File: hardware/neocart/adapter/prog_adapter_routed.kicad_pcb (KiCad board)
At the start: 2 copper layers, 174 x 134 mm, 79 parts, among them J1 FPGA_U2, J2 TO_CHA, J3 FPGA_U1, J4 microSD, U1 74LVC245, U10 74HC165, U2 74LVC245, U3 74LVC245, U4 74HC165, U5 74HC165, U6 74HC165, U7 74HC165, U8 74HC165, U9 74HC165

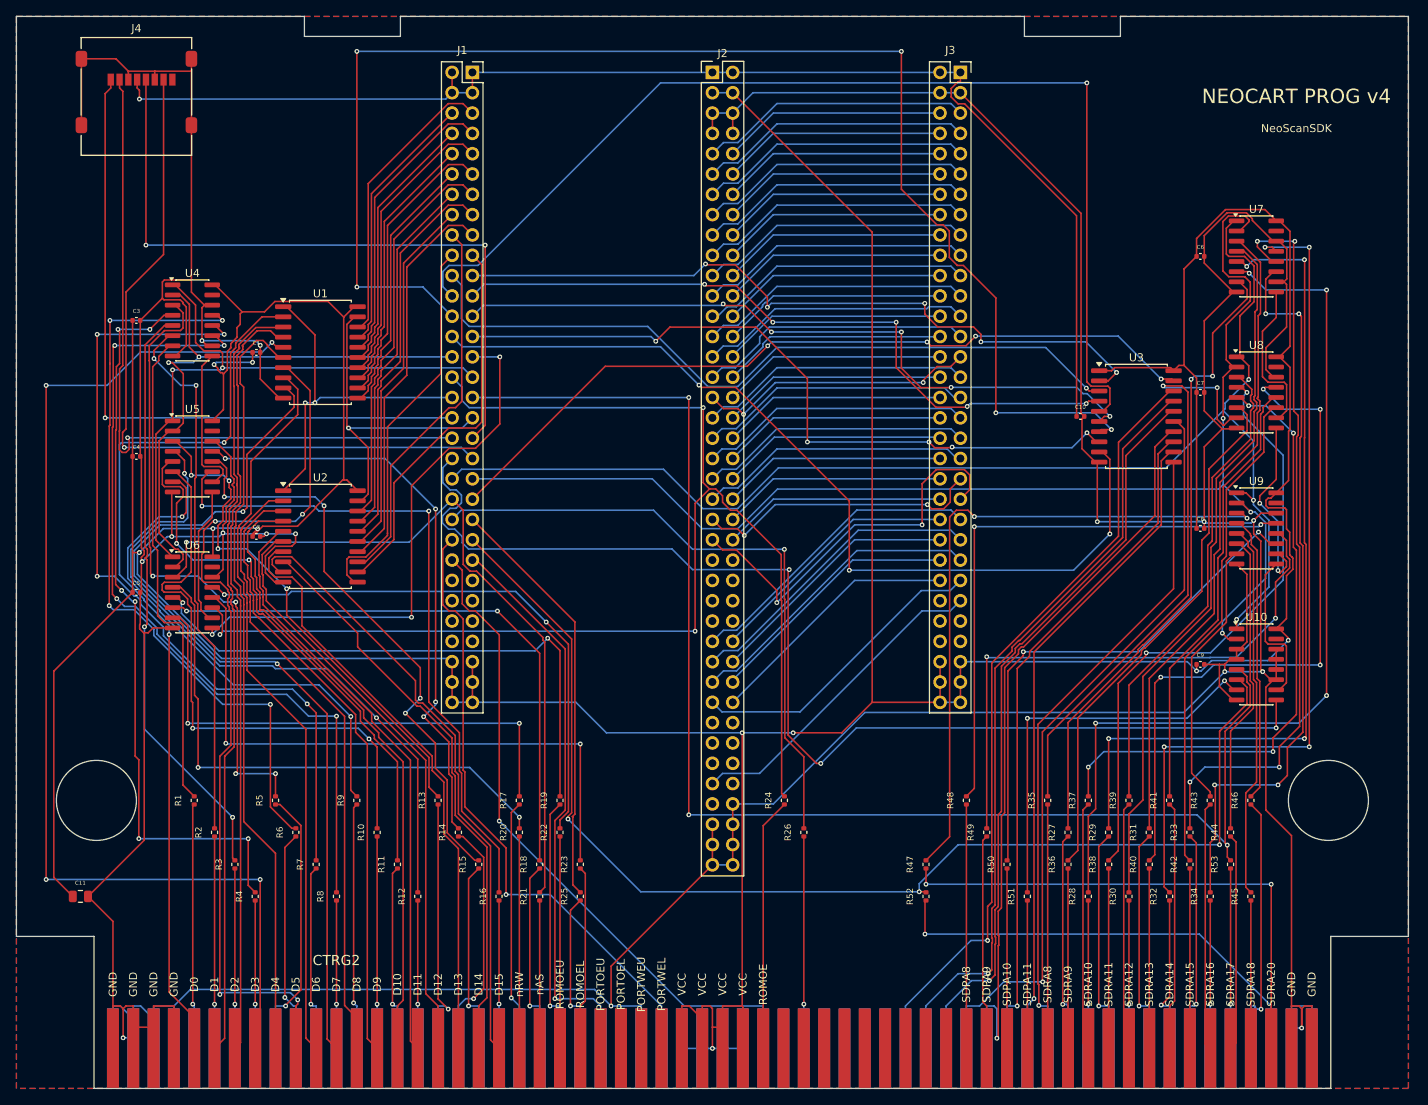
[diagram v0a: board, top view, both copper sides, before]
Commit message: NeoCart final routed PCBs + JLCPCB Gerbers — ready to order
Fixed J1 GND pins (60,62,64) from QMTech schematic — FPGA now has
ground through both headers. Re-routed with Freerouting 2.0.1 (Java 21,
multi-thread). GND routed as signal net, not just copper pour.

DRC clean:
- PROG: 143 violations (121 gold finger edge + 22 text cosmetic), 0 unconnected
- CHA:  152 violations (120 gold finger edge + 32 cosmetic), 0 unconnected
- 0 starved thermals, 0 shorts, 0 clearance errors

Chip verification: all 10 ICs power correct, all signal pins connected,
J1 GND confirmed on pins 60/62/64, J2 aligned between boards.

Gerbers: neocart_prog_gerbers.zip, neocart_cha_gerbers.zip
Order settings: 2-layer, 1.6mm, ENIG, gold fingers Yes, 45° chamfer.

Co-Authored-By: Claude Opus 4.6 (1M context) <noreply@anthropic.com>
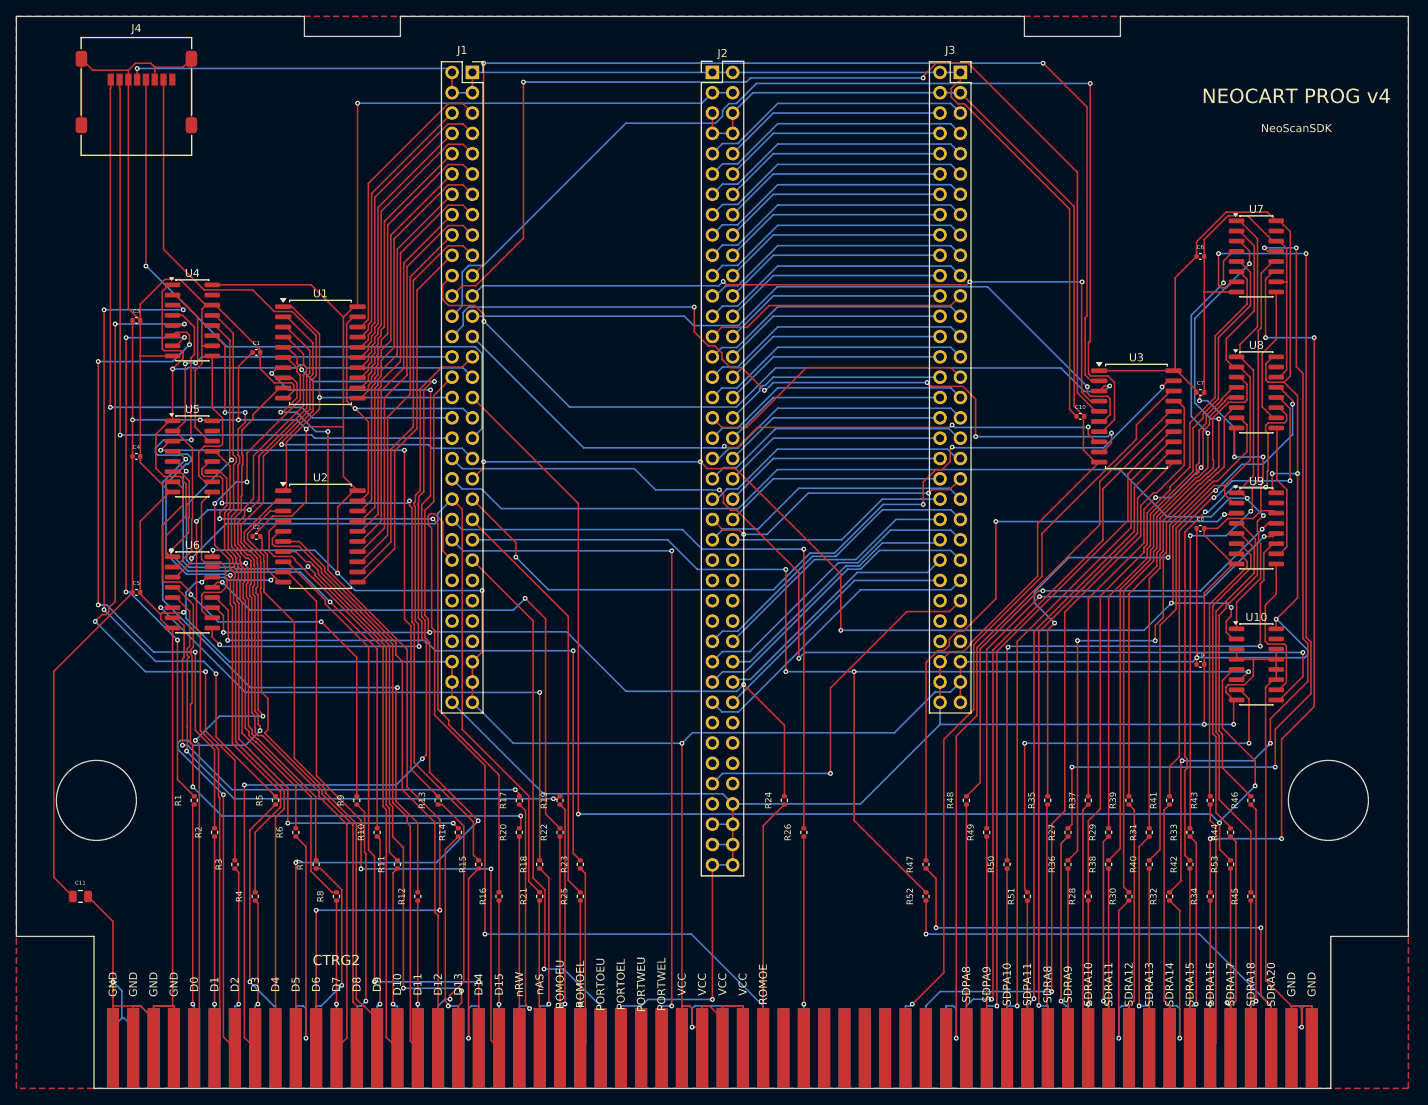
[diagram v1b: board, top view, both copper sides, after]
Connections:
- J1 pad 60: VCC_5V -> GND
- J1 pad 62: VCC_5V -> GND
- J1 pad 64: VCC_5V -> GND
- J3 pad 60: VCC_5V -> GND
- J3 pad 62: VCC_5V -> GND
- J3 pad 64: VCC_5V -> GND
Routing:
- net FSD0: track 91.9 -> 140.5 mm, vias 5 -> 2
- net ROMOE_R: track 170.0 -> 122.1 mm
- net GND: track 821.5 -> 868.1 mm, vias 15 -> 11
- net SDRA0_R: track 79.7 -> 117.2 mm, vias 2 -> 4
- net FSD5: track 178.9 -> 142.0 mm, vias 5 -> 1
- net SDRA1_R: track 114.7 -> 86.6 mm, vias 4 -> 0
- net SDRA2_R: track 104.8 -> 79.2 mm, vias 4 -> 0
- net A6_R: track 94.1 -> 69.8 mm, vias 4 -> 0
- net A8_R: track 103.8 -> 79.9 mm, vias 4 -> 2
- net 4MB: track 83.4 -> 106.6 mm
- net A7_R: track 101.9 -> 81.5 mm, vias 4 -> 2
- net D6: track 92.0 -> 111.9 mm, vias 0 -> 4
- net D7: track 111.2 -> 92.5 mm, vias 2 -> 0
- net SDRA10_R: track 77.7 -> 59.3 mm, vias 4 -> 2
- net A2_R: track 67.2 -> 83.9 mm, vias 2 -> 4
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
